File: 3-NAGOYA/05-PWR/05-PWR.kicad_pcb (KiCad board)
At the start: 2 copper layers, 90 x 90 mm, 23 parts, among them J1 voltmeter, J2 Battery, Q1 Q_PMOS_GDS, SW1 SW_SPST

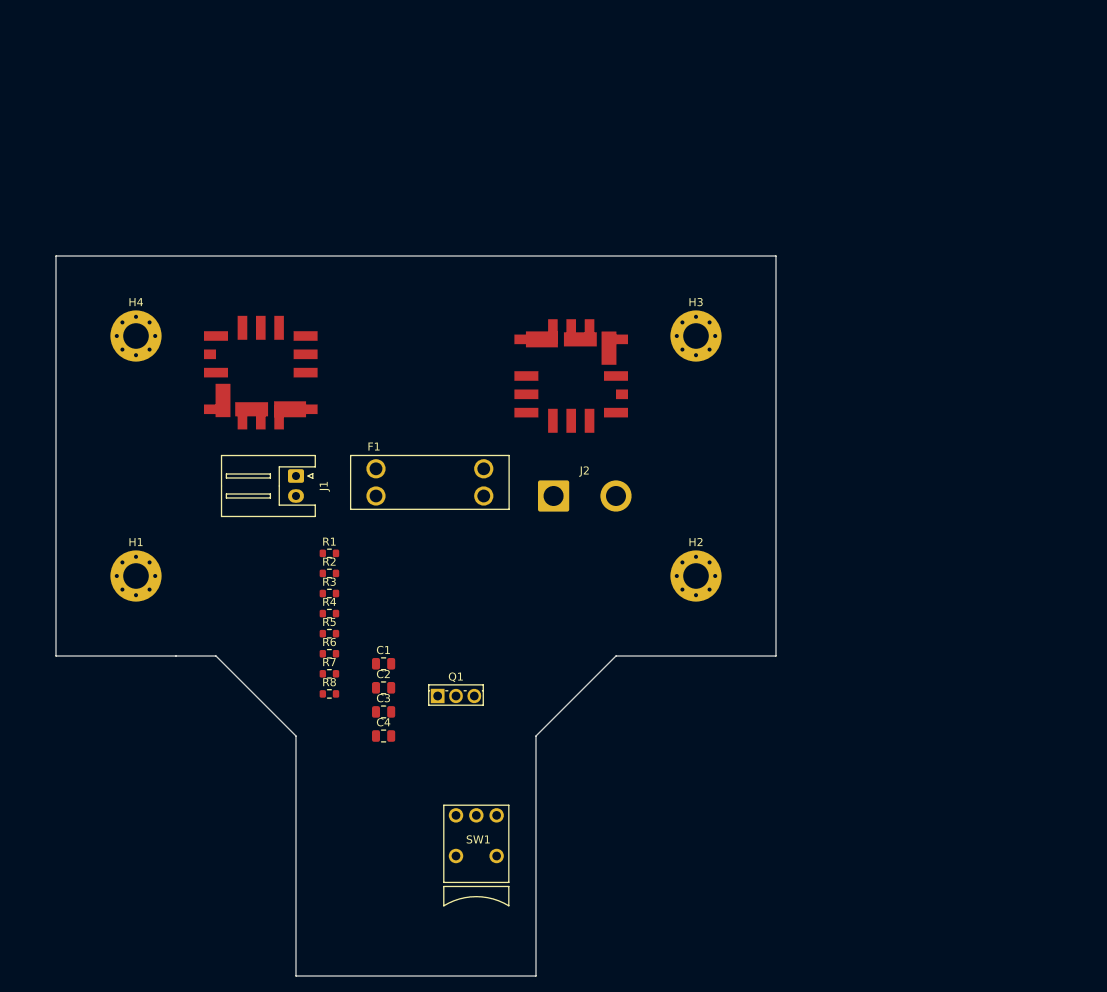
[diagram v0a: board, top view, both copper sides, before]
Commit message: 01-MAIN回路図終わり
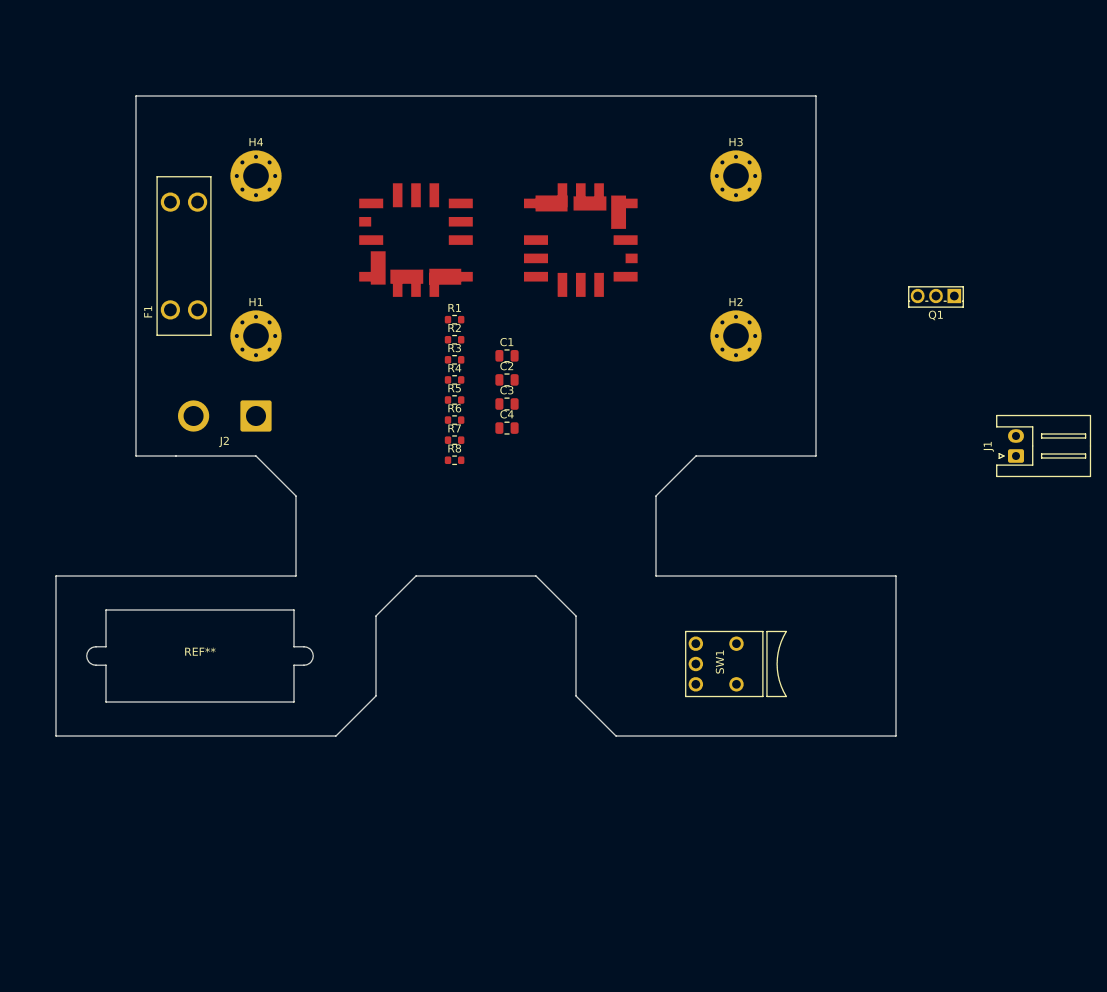
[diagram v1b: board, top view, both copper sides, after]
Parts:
- added REF**: voltmeter, Akiduki:Voltmeter, F.Cu at (38.0, 140.0)
- moved J1 90.0 mm to (140.0, 115.0), turned to 90 degrees
- moved Q1 81.7 mm to (132.3, 95.0), turned to 180 degrees
- moved F1 41.8 mm to (36.0, 90.0), turned to 90 degrees
- moved C3 41.5 mm to (76.4, 108.5)
- moved C1 41.5 mm to (76.4, 102.5)
- moved C2 41.5 mm to (76.4, 105.5)
- moved C4 41.5 mm to (76.4, 111.5)
- moved J2 38.5 mm to (45.0, 110.0), turned to 180 degrees
- moved H1 33.5 mm to (45.0, 100.0)
- moved SW1 33.3 mm to (100.0, 141.0), turned to 90 degrees
- moved R1 33.1 mm to (69.8, 98.0)
- moved R2 33.1 mm to (69.8, 100.5)
- moved R5 33.1 mm to (69.8, 108.0)
- moved R8 33.1 mm to (69.8, 115.5)
- moved R3 33.1 mm to (69.8, 103.0)
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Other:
- board size 90 x 90 mm -> 105 x 80 mm

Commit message: 01-MAIN部品配置完了
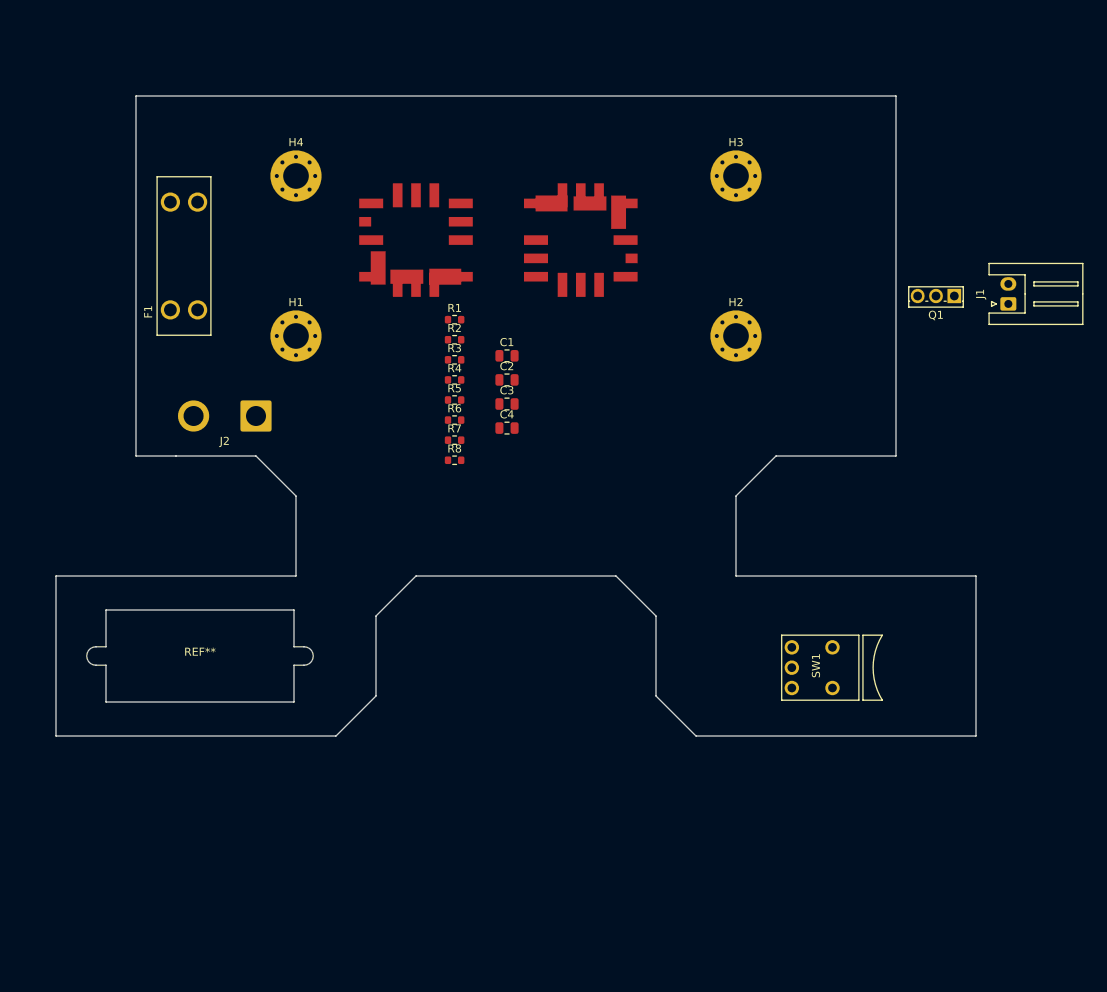
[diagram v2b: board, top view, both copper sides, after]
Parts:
- moved J1 19.0 mm to (139.0, 96.0)
- moved SW1 12.0 mm to (112.0, 141.5)
- moved H1 5.00 mm to (50.0, 100.0)
- moved H4 5.00 mm to (50.0, 80.0)
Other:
- board size 105 x 80 mm -> 115 x 80 mm
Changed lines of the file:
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@@
   )
   (footprint "MountingHole:MountingHole_3.2mm_M3_Pad_Via" (layer "F.Cu")
-    (at 45 80)
+    (at 50 80)
     (descr "Mounting Hole 3.2mm, M3")
     (tags "mounting hole 3.2mm m3")
@@
   )
   (footprint "Akiduki:AkizukiSmallRockerSwitchHorizontal" (layer "F.Cu")
-    (at 99.979859 141 90)
+    (at 111.979859 141.46 90)
     (property "LCSC" "")
     (property "Sheetfile" "05-PWR.kicad_sch")
@@
   )
   (footprint "MountingHole:MountingHole_3.2mm_M3_Pad_Via" (layer "F.Cu")
-    (at 45 100)
+    (at 50 100)
     (descr "Mounting Hole 3.2mm, M3")
     (tags "mounting hole 3.2mm m3")
@@
   )
   (footprint "Connector_JST:JST_XH_S2B-XH-A_1x02_P2.50mm_Horizontal" (layer "F.Cu")
-    (at 140 115 90)
+    (at 139.044 95.992 90)
     (descr "JST XH series connector, S2B-XH-A (http://www.jst-mfg.com/product/pdf/eng/eXH.pdf), generated with kicad-footprint-generator")
     (tags "connector JST XH horizontal")
@@
     )
   )
-  (gr_line (start 115 70) (end 30 70)
-    (stroke (width 0.1) (type default)) (layer "Edge.Cuts"))
-  (gr_line (start 85 145) (end 90 150)
-    (stroke (width 0.1) (type default)) (layer "Edge.Cuts"))
-  (gr_line (start 80 130) (end 85 135)
+  (gr_line (start 125 70) (end 30 70)
+    (stroke (width 0.1) (type default)) (layer "Edge.Cuts"))
+  (gr_line (start 95 145) (end 100 150)
+    (stroke (width 0.1) (type default)) (layer "Edge.Cuts"))
+  (gr_line (start 90 130) (end 95 135)
     (stroke (width 0.1) (type default)) (layer "Edge.Cuts"))
   (gr_line (start 20 130) (end 50 130)
@@
   (gr_line (start 20 150) (end 55 150)
     (stroke (width 0.1) (type default)) (layer "Edge.Cuts"))
-  (gr_line (start 65 130) (end 80 130)
-    (stroke (width 0.1) (type default)) (layer "Edge.Cuts"))
-  (gr_line (start 115 115) (end 115 70)
-    (stroke (width 0.1) (type default)) (layer "Edge.Cuts"))
-  (gr_line (start 90 150) (end 125 150)
-    (stroke (width 0.1) (type default)) (layer "Edge.Cuts"))
-  (gr_line (start 100 115) (end 115 115)
+  (gr_line (start 65 130) (end 90 130)
+    (stroke (width 0.1) (type default)) (layer "Edge.Cuts"))
+  (gr_line (start 125 115) (end 125 70)
+    (stroke (width 0.1) (type default)) (layer "Edge.Cuts"))
+  (gr_line (start 100 150) (end 135 150)
+    (stroke (width 0.1) (type default)) (layer "Edge.Cuts"))
+  (gr_line (start 110 115) (end 125 115)
     (stroke (width 0.1) (type default)) (layer "Edge.Cuts"))
   (gr_line (start 35 115) (end 45 115)
@@
   (gr_line (start 45 115) (end 50 120)
     (stroke (width 0.1) (type default)) (layer "Edge.Cuts"))
-  (gr_line (start 95 120) (end 95 130)
+  (gr_line (start 105 120) (end 105 130)
     (stroke (width 0.1) (type default)) (layer "Edge.Cuts"))
   (gr_line (start 50 120) (end 50 130)
@@
   (gr_line (start 60 135) (end 65 130)
     (stroke (width 0.1) (type default)) (layer "Edge.Cuts"))
-  (gr_line (start 85 135) (end 85 145)
-    (stroke (width 0.1) (type default)) (layer "Edge.Cuts"))
-  (gr_line (start 125 130) (end 125 150)
+  (gr_line (start 95 135) (end 95 145)
+    (stroke (width 0.1) (type default)) (layer "Edge.Cuts"))
+  (gr_line (start 135 130) (end 135 150)
     (stroke (width 0.1) (type default)) (layer "Edge.Cuts"))
   (gr_line (start 60 145) (end 60 135)
@@
   (gr_line (start 30 70) (end 30 115)
     (stroke (width 0.1) (type default)) (layer "Edge.Cuts"))
-  (gr_line (start 95 130) (end 125 130)
-    (stroke (width 0.1) (type default)) (layer "Edge.Cuts"))
-  (gr_line (start 100 115) (end 95 120)
+  (gr_line (start 105 130) (end 135 130)
+    (stroke (width 0.1) (type default)) (layer "Edge.Cuts"))
+  (gr_line (start 110 115) (end 105 120)
     (stroke (width 0.1) (type default)) (layer "Edge.Cuts"))
   (gr_line (start 35 115) (end 30 115)

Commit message: 04-RESCUE完了。全基板あとシルクだけ
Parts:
- J1: footprint Connector_JST:JST_XH_S2B-XH-A_1x02_P2.50mm_Horizontal -> Connector_Wire:SolderWire-0.5sqmm_1x02_P4.6mm_D0.9mm_OD2.1mm
- moved J1 102.2 mm to (43.4, 132.1), turned to 0 degrees
- moved Q1 90.6 mm to (42.4, 83.8), turned to -90 degrees
- moved R8 45.2 mm to (38.2, 83.2)
- moved R5 39.0 mm to (98.3, 81.3), turned to -90 degrees
- moved R4 38.7 mm to (97.5, 78.5)
- moved C4 33.3 mm to (60.3, 82.3), turned to -90 degrees
- moved R7 32.8 mm to (58.3, 82.3), turned to -90 degrees
- moved R6 29.6 mm to (79.6, 82.6), turned to -90 degrees
- moved R3 28.8 mm to (77.2, 75.2), turned to 90 degrees
- moved C3 26.4 mm to (81.5, 82.6), turned to -90 degrees
- moved R2 25.9 mm to (75.6, 75.2), turned to -90 degrees
- moved R1 23.1 mm to (73.9, 75.2), turned to 90 degrees
- moved C1 22.3 mm to (60.3, 87.0), turned to 90 degrees
- moved C2 18.8 mm to (81.5, 87.4), turned to 90 degrees
- moved J2 8.02 mm to (37.0, 109.5), turned to 0 degrees
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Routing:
- net Net-(Q1-G): track 0.00 -> 190.4 mm
- net VDD: track 0.00 -> 91.7 mm, vias 0 -> 4
- net GND: track 0.00 -> 43.7 mm, vias 0 -> 40
- net +5V: track 0.00 -> 11.2 mm
- net Net-(U2-Trim): track 0.00 -> 4.50 mm
- net +3V3: track 0.00 -> 4.09 mm
- net Net-(U1-Trim): track 0.00 -> 2.80 mm
- net Net-(R4-Pad2): track 0.00 -> 2.00 mm
- net Net-(R2-Pad2): track 0.00 -> 1.65 mm
- net Net-(R1-Pad2): track 0.00 -> 1.65 mm
- added copper zone on F.Cu, net +3V3
- added copper zone on F.Cu, net +5V
- added copper zone on B.Cu, net GND
- added copper zone on F.Cu, net GND
- added copper zone on B.Cu, net Net-(J2-Pin_1)
- added copper zone on F.Cu, net Net-(J2-Pin_1)
- added copper zone on B.Cu, net Net-(Q1-S)
- added copper zone on F.Cu, net Net-(Q1-S)
- added copper zone on B.Cu, net VDD
- added copper zone on F.Cu, net VDD

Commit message: つかれた
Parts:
- added G***: LOGO, logo:st_logo_middle, F.Cu at (73.8, 108.7)
- added G***: LOGO, logo:tuton_logo, F.Cu at (57.9, 107.8)
- added G***: LOGO, logo:jlcpcb_logo_big, F.Cu at (98.8, 107.8)
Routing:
- net VDD: track 91.7 -> 90.6 mm
- net GND: vias 40 -> 43
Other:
- board text added: "10A Fuse"
- board text added: "3V3"
- board text added: "5V"
- board text added: "D"
- board text added: "G"
- board text added: "GND"
- board text added: "Pch MOSFET"
- board text added: "S"
- board text added: "SW"
- board text added: "Trim"
- board text added: "Tuton NAGOYA 05-PWR"
- board text added: "VBAT"
- board text added: "VDD"
- board text added: "VOLTMETER"
- board text added: "x"
